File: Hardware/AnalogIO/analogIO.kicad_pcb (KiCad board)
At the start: 4 copper layers, 70 x 66.8 mm, 2 parts, among them J1 Conn_02x23_Odd_Even, J3 Conn_02x23_Odd_Even

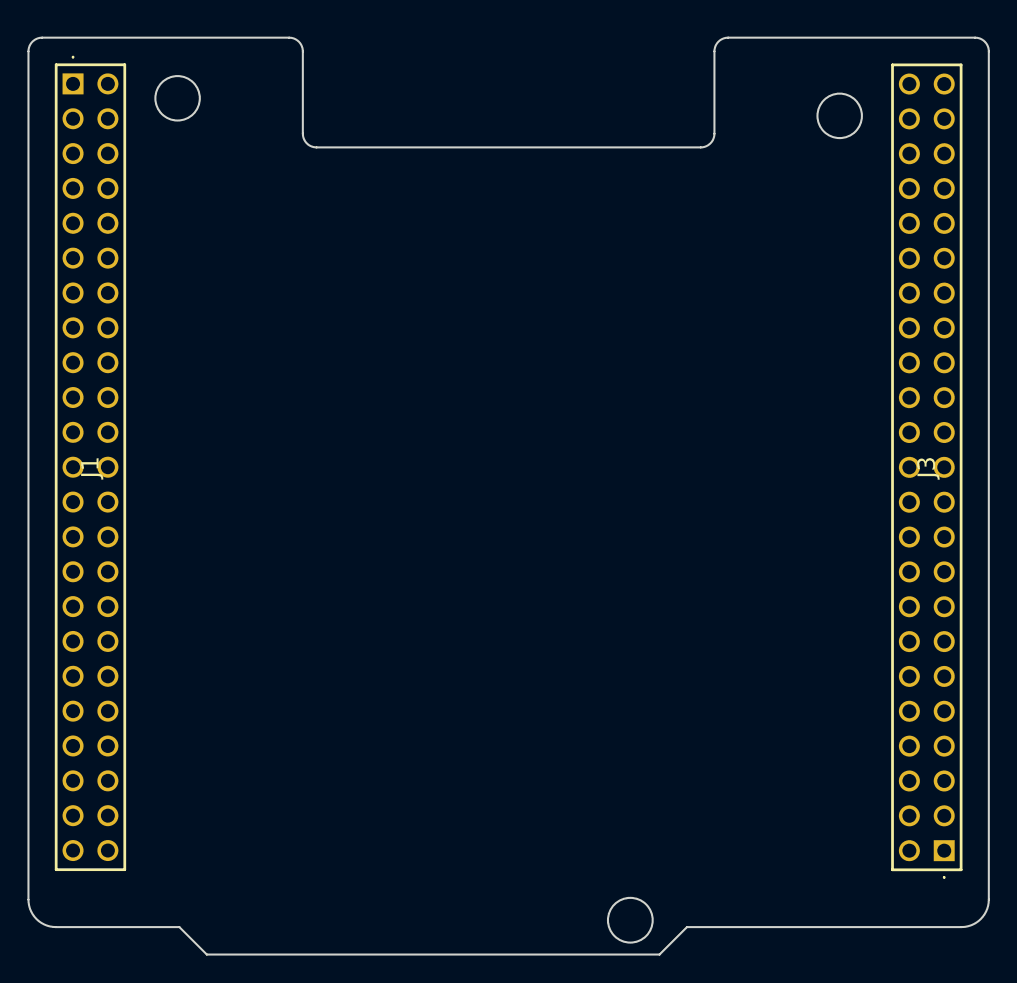
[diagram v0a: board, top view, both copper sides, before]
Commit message: schematic update - digital and analog footprints added
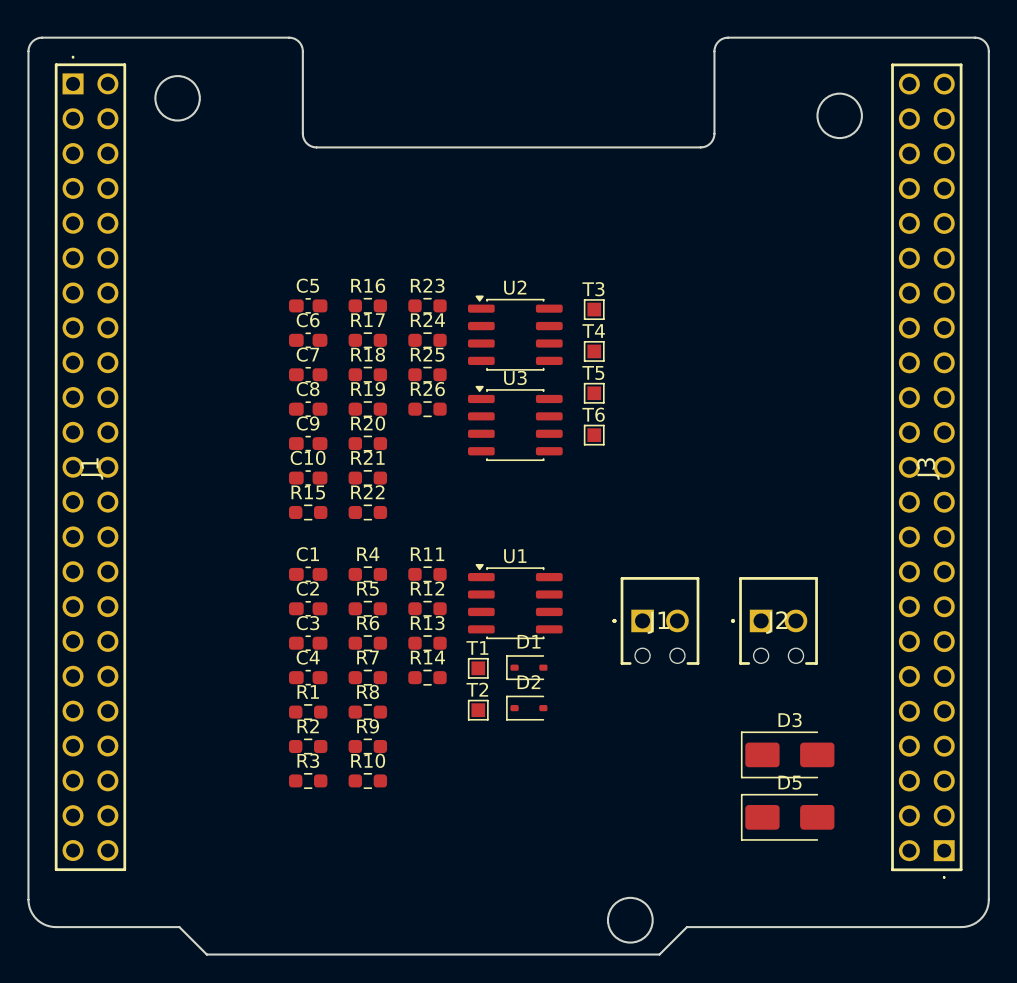
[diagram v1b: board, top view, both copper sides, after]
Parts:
- added C1: 100n, Capacitor_SMD:C_0603_1608Metric_Pad1.08x0.95mm_HandSolder, F.Cu at (136.4, 88.3)
- added C10: 100n, Capacitor_SMD:C_0603_1608Metric_Pad1.08x0.95mm_HandSolder, F.Cu at (136.4, 81.3)
- added C2: 100n, Capacitor_SMD:C_0603_1608Metric_Pad1.08x0.95mm_HandSolder, F.Cu at (136.4, 90.8)
- added C3: 100n, Capacitor_SMD:C_0603_1608Metric_Pad1.08x0.95mm_HandSolder, F.Cu at (136.4, 93.3)
- added C4: 100n, Capacitor_SMD:C_0603_1608Metric_Pad1.08x0.95mm_HandSolder, F.Cu at (136.4, 95.8)
- added C5: 100n, Capacitor_SMD:C_0603_1608Metric_Pad1.08x0.95mm_HandSolder, F.Cu at (136.4, 68.7)
- added C6: 100n, Capacitor_SMD:C_0603_1608Metric_Pad1.08x0.95mm_HandSolder, F.Cu at (136.4, 71.2)
- added C7: 100n, Capacitor_SMD:C_0603_1608Metric_Pad1.08x0.95mm_HandSolder, F.Cu at (136.4, 73.7)
- added C8: 100n, Capacitor_SMD:C_0603_1608Metric_Pad1.08x0.95mm_HandSolder, F.Cu at (136.4, 76.2)
- added C9: 100n, Capacitor_SMD:C_0603_1608Metric_Pad1.08x0.95mm_HandSolder, F.Cu at (136.4, 78.8)
- added D1: BZX384C3V6, Diode_SMD:D_SOD-323, F.Cu at (152.5, 95.1)
- added D2: BZX384C3V6, Diode_SMD:D_SOD-323, F.Cu at (152.5, 98.0)
- added D3: SMAJ15CA, Diode_SMD:D_SMA, F.Cu at (171.5, 101.5)
- added D5: SMAJ15CA, Diode_SMD:D_SMA, F.Cu at (171.5, 106.0)
- added J1: ANALOG INPUTS, PLC_STM:1725656, F.Cu at (160.8, 91.7)
- added J2: ANALOG OUTPUTS, PLC_STM:1725656, F.Cu at (169.4, 91.7)
- added R1: 100k, Resistor_SMD:R_0603_1608Metric_Pad0.98x0.95mm_HandSolder, F.Cu at (136.4, 98.3)
- added R10: 10k, Resistor_SMD:R_0603_1608Metric_Pad0.98x0.95mm_HandSolder, F.Cu at (140.7, 103.3)
- added R11: 10k, Resistor_SMD:R_0603_1608Metric_Pad0.98x0.95mm_HandSolder, F.Cu at (145.1, 88.3)
- added R12: 10k, Resistor_SMD:R_0603_1608Metric_Pad0.98x0.95mm_HandSolder, F.Cu at (145.1, 90.8)
- added R13: 1k, Resistor_SMD:R_0603_1608Metric_Pad0.98x0.95mm_HandSolder, F.Cu at (145.1, 93.3)
- added R14: 1k, Resistor_SMD:R_0603_1608Metric_Pad0.98x0.95mm_HandSolder, F.Cu at (145.1, 95.8)
- added R15: 33k, Resistor_SMD:R_0603_1608Metric_Pad0.98x0.95mm_HandSolder, F.Cu at (136.4, 83.8)
- added R16: 33k, Resistor_SMD:R_0603_1608Metric_Pad0.98x0.95mm_HandSolder, F.Cu at (140.7, 68.7)
- added R17: 470R, Resistor_SMD:R_0603_1608Metric_Pad0.98x0.95mm_HandSolder, F.Cu at (140.7, 71.2)
- added R18: 470R, Resistor_SMD:R_0603_1608Metric_Pad0.98x0.95mm_HandSolder, F.Cu at (140.7, 73.7)
- added R19: 10k, Resistor_SMD:R_0603_1608Metric_Pad0.98x0.95mm_HandSolder, F.Cu at (140.7, 76.2)
- added R2: 100k, Resistor_SMD:R_0603_1608Metric_Pad0.98x0.95mm_HandSolder, F.Cu at (136.4, 100.8)
- added R20: 10k, Resistor_SMD:R_0603_1608Metric_Pad0.98x0.95mm_HandSolder, F.Cu at (140.7, 78.8)
- added R21: 15k4, Resistor_SMD:R_0603_1608Metric_Pad0.98x0.95mm_HandSolder, F.Cu at (140.7, 81.3)
- added R22: 15k4, Resistor_SMD:R_0603_1608Metric_Pad0.98x0.95mm_HandSolder, F.Cu at (140.7, 83.8)
- added R23: 1k, Resistor_SMD:R_0603_1608Metric_Pad0.98x0.95mm_HandSolder, F.Cu at (145.1, 68.7)
- added R24: 1k, Resistor_SMD:R_0603_1608Metric_Pad0.98x0.95mm_HandSolder, F.Cu at (145.1, 71.2)
- added R25: 100k, Resistor_SMD:R_0603_1608Metric_Pad0.98x0.95mm_HandSolder, F.Cu at (145.1, 73.7)
- added R26: 100k, Resistor_SMD:R_0603_1608Metric_Pad0.98x0.95mm_HandSolder, F.Cu at (145.1, 76.2)
- added R3: 1k, Resistor_SMD:R_0603_1608Metric_Pad0.98x0.95mm_HandSolder, F.Cu at (136.4, 103.3)
- added R4: 1k, Resistor_SMD:R_0603_1608Metric_Pad0.98x0.95mm_HandSolder, F.Cu at (140.7, 88.3)
- added R5: 20k3, Resistor_SMD:R_0603_1608Metric_Pad0.98x0.95mm_HandSolder, F.Cu at (140.7, 90.8)
- added R6: 20k3, Resistor_SMD:R_0603_1608Metric_Pad0.98x0.95mm_HandSolder, F.Cu at (140.7, 93.3)
- added R7: 20k3, Resistor_SMD:R_0603_1608Metric_Pad0.98x0.95mm_HandSolder, F.Cu at (140.7, 95.8)
- added R8: 20k3, Resistor_SMD:R_0603_1608Metric_Pad0.98x0.95mm_HandSolder, F.Cu at (140.7, 98.3)
- added R9: 10k, Resistor_SMD:R_0603_1608Metric_Pad0.98x0.95mm_HandSolder, F.Cu at (140.7, 100.8)
- added T1: AI0, TestPoint:TestPoint_Pad_1.0x1.0mm, F.Cu at (148.8, 95.1)
- added T2: AI1, TestPoint:TestPoint_Pad_1.0x1.0mm, F.Cu at (148.8, 98.2)
- added T3: AO0_OUT, TestPoint:TestPoint_Pad_1.0x1.0mm, F.Cu at (157.2, 69.0)
- added T4: AO1_OUT, TestPoint:TestPoint_Pad_1.0x1.0mm, F.Cu at (157.2, 72.0)
- added T5: AO0_BUFF, TestPoint:TestPoint_Pad_1.0x1.0mm, F.Cu at (157.2, 75.1)
- added T6: AO1_BUFF, TestPoint:TestPoint_Pad_1.0x1.0mm, F.Cu at (157.2, 78.1)
- added U1: LM358, Package_SO:SOIC-8_3.9x4.9mm_P1.27mm, F.Cu at (151.5, 90.4)
- added U2: LM358, Package_SO:SOIC-8_3.9x4.9mm_P1.27mm, F.Cu at (151.5, 70.8)
- added U3: LM358, Package_SO:SOIC-8_3.9x4.9mm_P1.27mm, F.Cu at (151.5, 77.4)

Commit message: schematic update & pcb update
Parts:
- removed the J1 at (119.2, 52.5)
- added J4: NUCLEO RIGHT, PLC_STM:PRT12790, F.Cu at (180.2, 52.6)
- J3: value Conn_02x23_Odd_Even -> NUCLEO LEFT; footprint PLC_STM_Power:PRT12790 -> PLC_STM:PRT12790
- moved J3 84.6 mm to (119.3, 52.6), turned to -90 degrees
- moved D3 41.1 mm to (130.5, 102.5)
- moved R16 40.0 mm to (169.0, 97.0), turned to 90 degrees
- moved D1 39.5 mm to (130.6, 62.2), turned to 90 degrees
- moved R18 37.0 mm to (171.5, 94.3)
- moved R10 36.9 mm to (152.0, 68.2), turned to 180 degrees
- moved T2 36.7 mm to (145.8, 61.7)
- moved C7 36.4 mm to (162.1, 99.6)
- moved R22 36.2 mm to (175.4, 94.3)
- moved C10 36.2 mm to (172.0, 75.1), turned to 90 degrees
- moved R20 35.1 mm to (173.5, 91.4), turned to -90 degrees
- moved T1 34.8 mm to (139.0, 61.8)
- moved R9 34.8 mm to (132.8, 67.0)
- moved D2 34.7 mm to (154.3, 63.4), turned to 90 degrees
- moved C8 33.6 mm to (166.1, 92.1), turned to 180 degrees
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- renumbered D5 to D3, D3 to D4
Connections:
- net +12V renamed +15V
- net AO0 renamed AO_0
- net AO1 renamed AO_1
- C2 pad 1: -12V -> -15V
- C6 pad 1: -12V -> -15V
- C8 pad 1: -12V -> -15V
- J3 pad 10: unconnected-(J3-Pin_10-Pad10) -> UART5_TX
- J3 pad 11: unconnected-(J3-Pin_11-Pad11) -> GND
- J3 pad 12: unconnected-(J3-Pin_12-Pad12) -> UART5_RX
- J3 pad 13: unconnected-(J3-Pin_13-Pad13) -> GND
- J3 pad 15: unconnected-(J3-Pin_15-Pad15) -> +5V
- J3 pad 18: unconnected-(J3-Pin_18-Pad18) -> -15V
- J3 pad 22: unconnected-(J3-Pin_22-Pad22) -> UART2_RX
- J3 pad 24: unconnected-(J3-Pin_24-Pad24) -> UART2_TX
- J3 pad 30: unconnected-(J3-Pin_30-Pad30) -> GND
- J3 pad 39: unconnected-(J3-Pin_39-Pad39) -> GND
- J3 pad 41: unconnected-(J3-Pin_41-Pad41) -> CAN1_RX
- J3 pad 43: unconnected-(J3-Pin_43-Pad43) -> CAN1_TX
- J3 pad 6: unconnected-(J3-Pin_6-Pad6) -> UART4_TX
- J3 pad 7: unconnected-(J3-Pin_7-Pad7) -> +3V3
- J3 pad 8: unconnected-(J3-Pin_8-Pad8) -> UART4_RX
- J3 pad 9: unconnected-(J3-Pin_9-Pad9) -> +5V
- R13 pad 2: AI0 -> AI_0
- R14 pad 2: AI1 -> AI_1
- U1 pad 4: -12V -> -15V
- U2 pad 1: ANALOG_OUT0 -> ANALOG_OUT1
- U2 pad 2: /analog_output/OP_AO0- -> /analog_output/OP_AO1-
- U2 pad 3: /analog_output/OP_AO0_OUT -> /analog_output/OP_AO1_OUT
- U2 pad 4: -12V -> -15V
- U2 pad 5: /analog_output/OP_AO1_OUT -> /analog_output/OP_AO0_OUT
- U2 pad 6: /analog_output/OP_AO1- -> /analog_output/OP_AO0-
- U2 pad 7: ANALOG_OUT1 -> ANALOG_OUT0
- U3 pad 4: -12V -> -15V
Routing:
- net +15V: track 0.00 -> 122.5 mm, vias 0 -> 3
- net -15V: track 0.00 -> 102.9 mm, vias 0 -> 3
- net +5V: track 0.00 -> 95.1 mm, vias 0 -> 2
- net AI_0: track 0.00 -> 64.9 mm
- net ANALOG_IN1: track 0.00 -> 52.4 mm
- net +3V3: track 0.00 -> 47.3 mm, vias 0 -> 4
- net ANALOG_IN0: track 0.00 -> 41.6 mm
- net AO_0: track 0.00 -> 31.8 mm
- net ANALOG_OUT1: track 0.00 -> 30.3 mm
- net AI_1: track 0.00 -> 27.4 mm
- net GND: track 0.00 -> 25.2 mm, vias 0 -> 22
- net AO_1: track 0.00 -> 25.1 mm
- net /analog_output/OP_AO1_OUT: track 0.00 -> 23.9 mm
- net ANALOG_OUT0: track 0.00 -> 23.6 mm
- net /analog_output/OP_AO0_OUT: track 0.00 -> 23.3 mm
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- added copper zone on B.Cu, net GND
- added copper zone on F.Cu, net GND
- added copper zone on In1.Cu, net GND
- added copper zone on In2.Cu, net GND
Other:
- board size 70 x 66.8 mm -> 70 x 67.5 mm

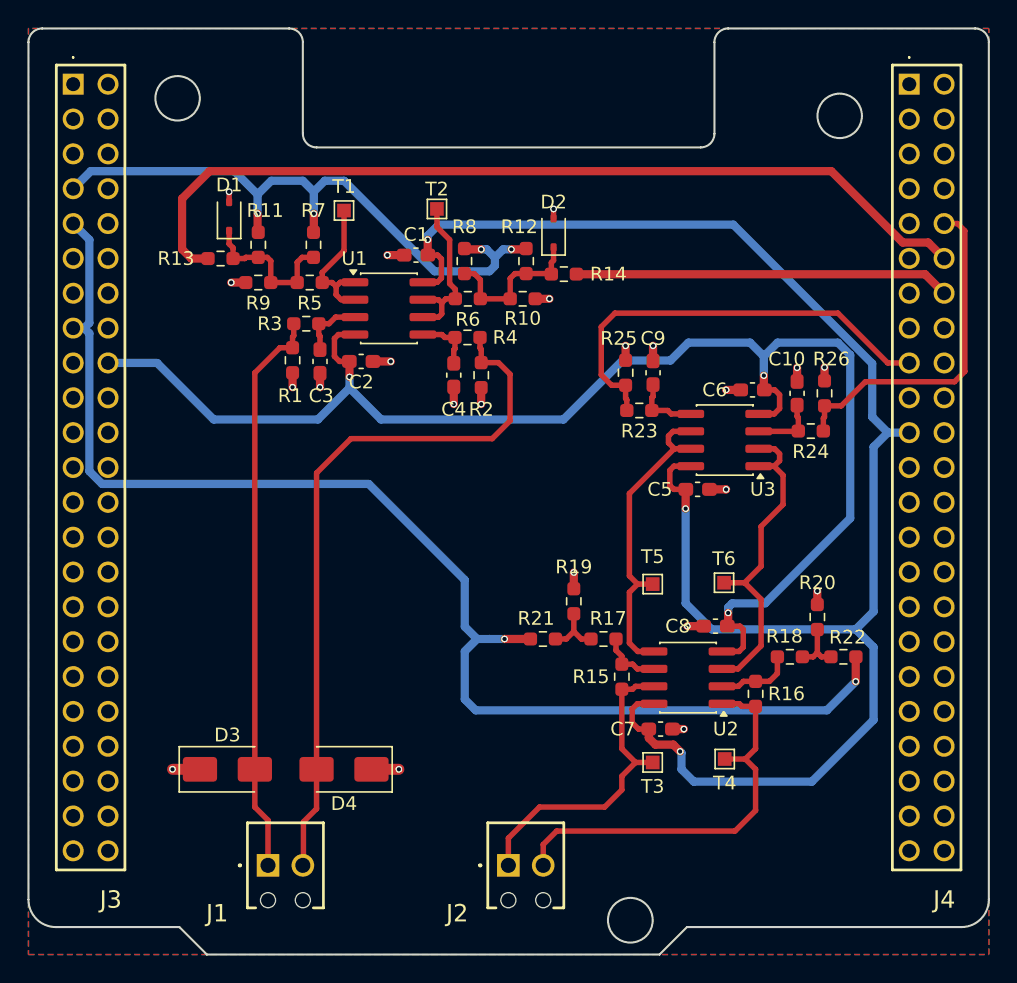
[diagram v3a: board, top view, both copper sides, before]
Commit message: analog & can finished
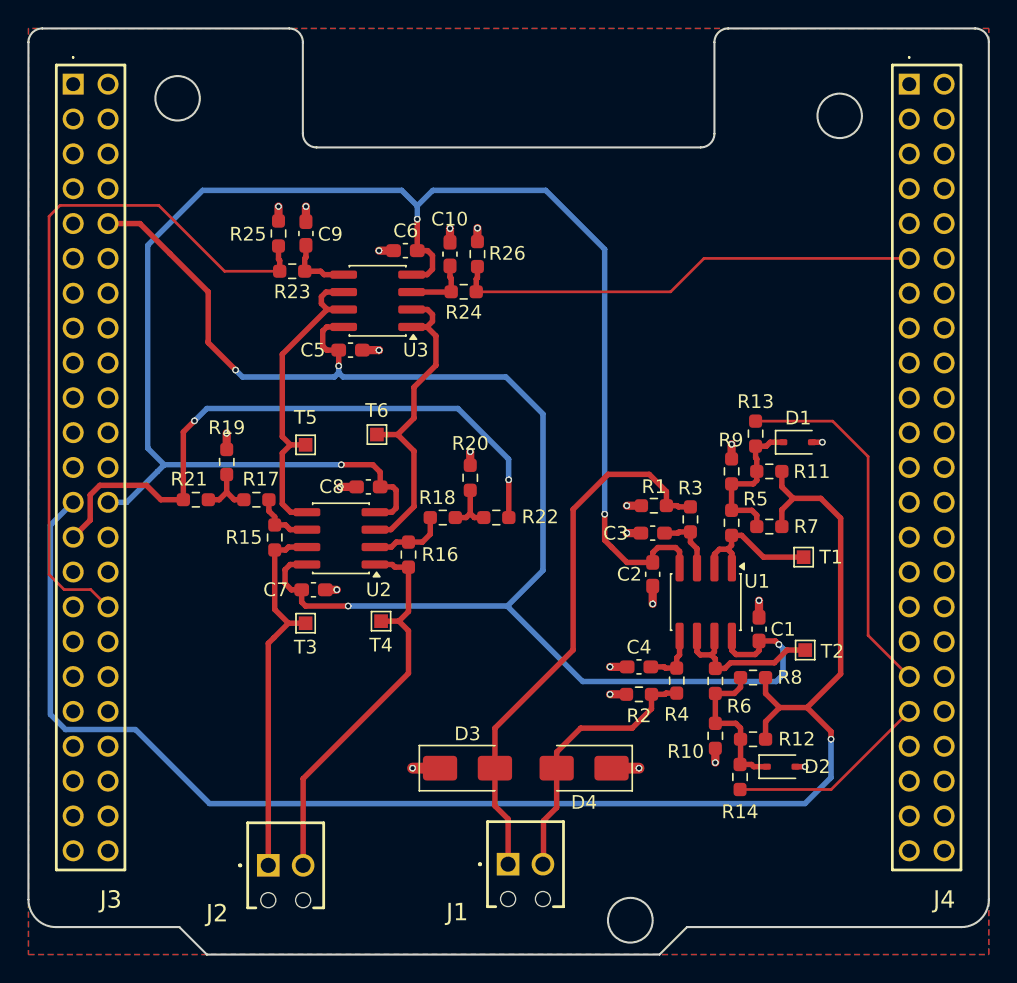
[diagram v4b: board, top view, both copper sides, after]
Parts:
- moved D1 44.6 mm to (172.1, 78.7), turned to 0 degrees
- moved D2 42.3 mm to (170.9, 102.3), turned to 0 degrees
- moved T1 42.0 mm to (172.5, 87.0), turned to -90 degrees
- moved T2 41.9 mm to (172.6, 93.8), turned to -90 degrees
- moved R13 41.0 mm to (169.0, 78.0), turned to 90 degrees
- moved R11 40.7 mm to (170.0, 80.8), turned to 0 degrees
- moved R7 39.1 mm to (170.0, 84.8), turned to 0 degrees
- moved R14 38.8 mm to (167.9, 103.1), turned to -90 degrees
- moved R12 38.6 mm to (168.8, 100.3), turned to 0 degrees
- moved R9 37.1 mm to (167.2, 80.8), turned to -90 degrees
- moved C1 37.0 mm to (169.2, 92.3), turned to 90 degrees
- moved R8 36.9 mm to (168.8, 95.8), turned to 0 degrees
- moved R5 35.4 mm to (167.2, 84.5), turned to 90 degrees
- moved R10 34.8 mm to (166.1, 100.1), turned to 90 degrees
- moved R6 33.2 mm to (166.1, 96.1), turned to -90 degrees
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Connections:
- J3 pad 10: UART5_TX -> +15V
- J3 pad 11: GND -> unconnected-(J3-Pin_11-Pad11)
- J3 pad 12: UART5_RX -> unconnected-(J3-Pin_12-Pad12)
- J3 pad 13: GND -> unconnected-(J3-Pin_13-Pad13)
- J3 pad 15: +5V -> unconnected-(J3-Pin_15-Pad15)
- J3 pad 18: -15V -> unconnected-(J3-Pin_18-Pad18)
- J3 pad 19: unconnected-(J3-Pin_19-Pad19) -> GND
- J3 pad 20: unconnected-(J3-Pin_20-Pad20) -> GND
- J3 pad 22: UART2_RX -> GND
- J3 pad 24: UART2_TX -> unconnected-(J3-Pin_24-Pad24)
- J3 pad 25: unconnected-(J3-Pin_25-Pad25) -> +3V3
- J3 pad 26: unconnected-(J3-Pin_26-Pad26) -> -15V
- J3 pad 27: unconnected-(J3-Pin_27-Pad27) -> +5V
- J3 pad 30: GND -> unconnected-(J3-Pin_30-Pad30)
- J3 pad 32: unconnected-(J3-Pin_32-Pad32) -> AO_0
- J3 pad 39: GND -> unconnected-(J3-Pin_39-Pad39)
- J3 pad 41: CAN1_RX -> unconnected-(J3-Pin_41-Pad41)
- J3 pad 43: CAN1_TX -> unconnected-(J3-Pin_43-Pad43)
- J3 pad 6: UART4_TX -> unconnected-(J3-Pin_6-Pad6)
- J3 pad 7: +3V3 -> unconnected-(J3-Pin_7-Pad7)
- J3 pad 8: UART4_RX -> unconnected-(J3-Pin_8-Pad8)
- J3 pad 9: +5V -> unconnected-(J3-Pin_9-Pad9)
- J4 pad 1: UART6_TX -> unconnected-(J4-Pin_1-Pad1)
- J4 pad 10: AO_1 -> unconnected-(J4-Pin_10-Pad10)
- J4 pad 11: UART6_TX -> AO_1
- J4 pad 12: AI_0 -> unconnected-(J4-Pin_12-Pad12)
- J4 pad 13: CAN2_RX -> unconnected-(J4-Pin_13-Pad13)
- J4 pad 14: AI_1 -> unconnected-(J4-Pin_14-Pad14)
- J4 pad 17: AO_0 -> unconnected-(J4-Pin_17-Pad17)
- J4 pad 2: CAN1_RX -> unconnected-(J4-Pin_2-Pad2)
- J4 pad 20: unconnected-(J4-Pin_20-Pad20) -> GND
- J4 pad 21: +15V -> unconnected-(J4-Pin_21-Pad21)
- J4 pad 23: AVDD -> unconnected-(J4-Pin_23-Pad23)
- J4 pad 25: AGND -> unconnected-(J4-Pin_25-Pad25)
- J4 pad 27: GND -> unconnected-(J4-Pin_27-Pad27)
- J4 pad 35: unconnected-(J4-Pin_35-Pad35) -> AI_0
- J4 pad 37: unconnected-(J4-Pin_37-Pad37) -> AI_1
- J4 pad 39: GND -> unconnected-(J4-Pin_39-Pad39)
- J4 pad 4: CAN1_TX -> unconnected-(J4-Pin_4-Pad4)
- J4 pad 40: UART6_TX -> unconnected-(J4-Pin_40-Pad40)
- J4 pad 42: UART6_RX -> unconnected-(J4-Pin_42-Pad42)
- J4 pad 44: UART5_TX -> unconnected-(J4-Pin_44-Pad44)
- J4 pad 46: UART5_RX -> unconnected-(J4-Pin_46-Pad46)
- J4 pad 5: CAN2_TX -> unconnected-(J4-Pin_5-Pad5)
- J4 pad 6: AVDD -> unconnected-(J4-Pin_6-Pad6)
- J4 pad 7: CAN2_RX -> unconnected-(J4-Pin_7-Pad7)
- J4 pad 8: GND -> unconnected-(J4-Pin_8-Pad8)
- J4 pad 9: unconnected-(J4-Pin_9-Pad9) -> GND
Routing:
- net +3V3: track 47.3 -> 113.3 mm, vias 4 -> 1
- net +5V: track 95.1 -> 46.3 mm
- net AI_0: track 64.9 -> 26.6 mm
- net ANALOG_IN1: track 52.4 -> 19.7 mm
- net AO_0: track 31.8 -> 52.4 mm
- net -15V: track 102.9 -> 117.4 mm
- net AI_1: track 27.4 -> 14.7 mm
- net +15V: track 122.5 -> 111.2 mm, vias 3 -> 4
- net AO_1: track 25.1 -> 34.4 mm
- net ANALOG_OUT0: track 23.6 -> 27.7 mm
- net ANALOG_IN0: track 41.6 -> 39.8 mm
- net ANALOG_OUT1: track 30.3 -> 29.3 mm
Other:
- board text removed: "®©®"
